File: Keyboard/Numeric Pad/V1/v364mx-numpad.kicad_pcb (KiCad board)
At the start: 2 copper layers, 83.1 x 140.3 mm, 20 parts, among them J9 KEYPAD2, SW193 KP"0", SW29 KP "@", SW30 KP "+", SW31 KP "-" was KP "*", SW32 KP "=", SW45 KP "7", SW46 KP "8", SW47 KP "9", SW48 KP "*", SW61 KP "4", SW62 KP "5", SW63 KP "6", SW64 KP "/", SW77 KP "1", SW78 KP "2", SW79 KP "3", SW80 "ENTER", SW94 KP ".", SW95 KP ":" was KP "00"

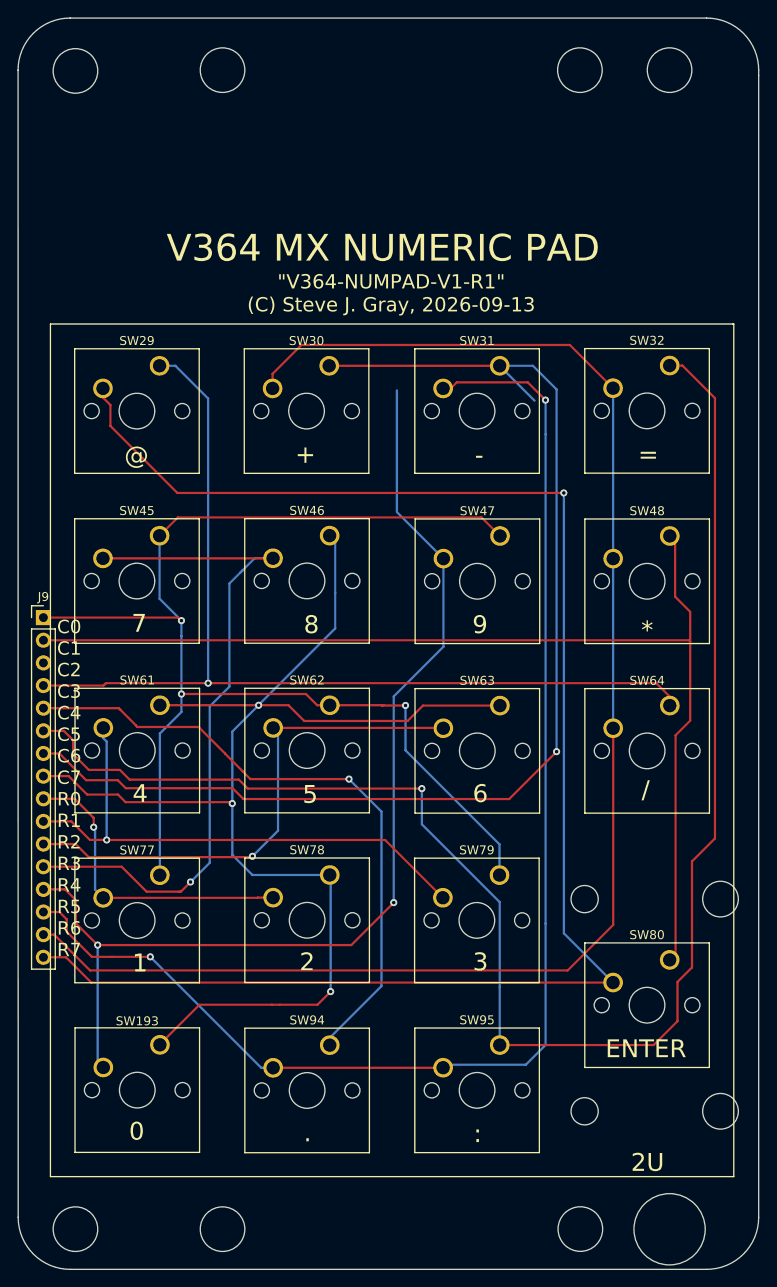
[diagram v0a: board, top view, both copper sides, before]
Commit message: Fix Numpad V1R1, add gerbers
Fixed some DRC errors, missing traces on schematic and added gerbers. NOTE: V1R2 is available and recommended over this V1R1 update as it gives you the choice to use regular or low-profile switches.
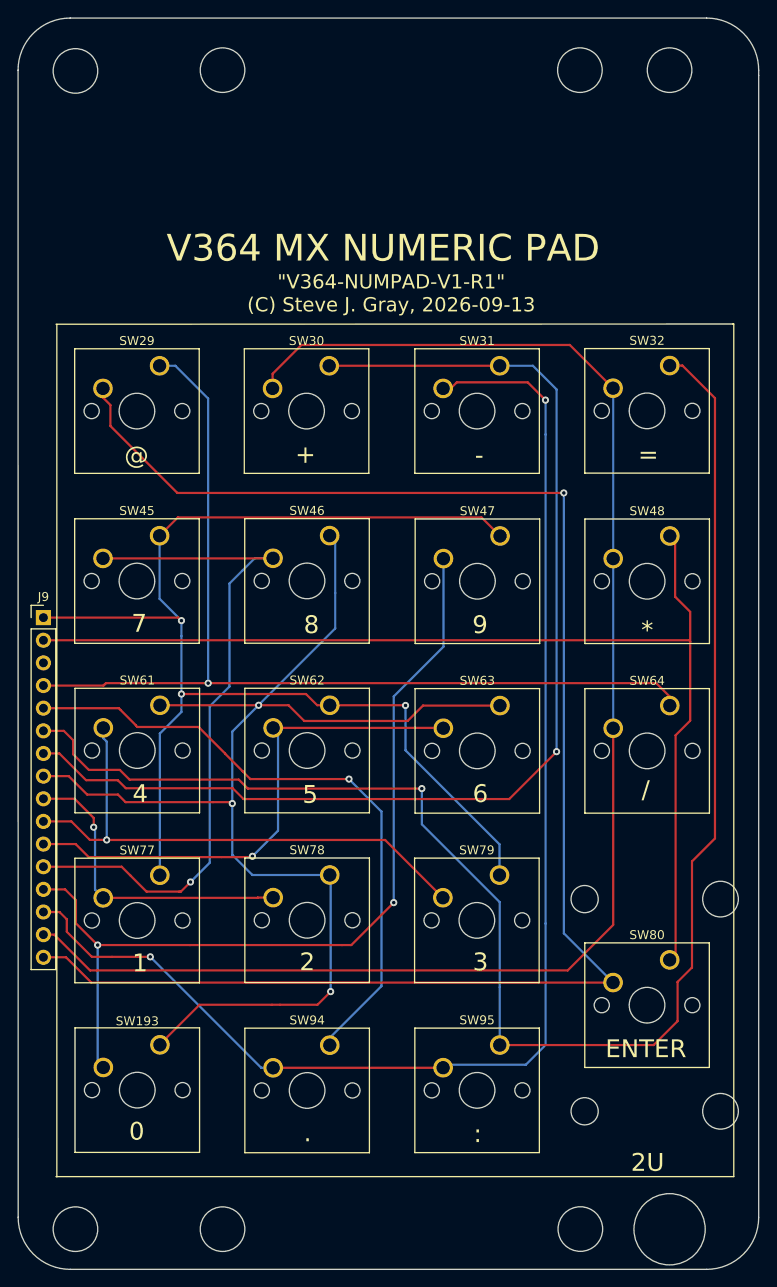
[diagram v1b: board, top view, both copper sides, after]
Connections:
- SW61 pad 2: unconnected-(SW61-Pad2) -> R1
- SW63 pad 2: unconnected-(SW63-Pad2) -> R2
- SW78 pad 2: unconnected-(SW78-Pad2) -> R0
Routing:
- net R4: track 121.3 -> 100.3 mm
- net C6: track 134.6 -> 129.1 mm
